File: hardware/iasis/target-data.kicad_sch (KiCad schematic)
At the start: 22 parts, among them J401 1054500101, U401 HD3SS3212IRKSR, U402 TPD4E02B04DQAR, U403 TPD4E02B04DQAR, U404 TPD6S300ARUKR, U405 FUSB302BMPX

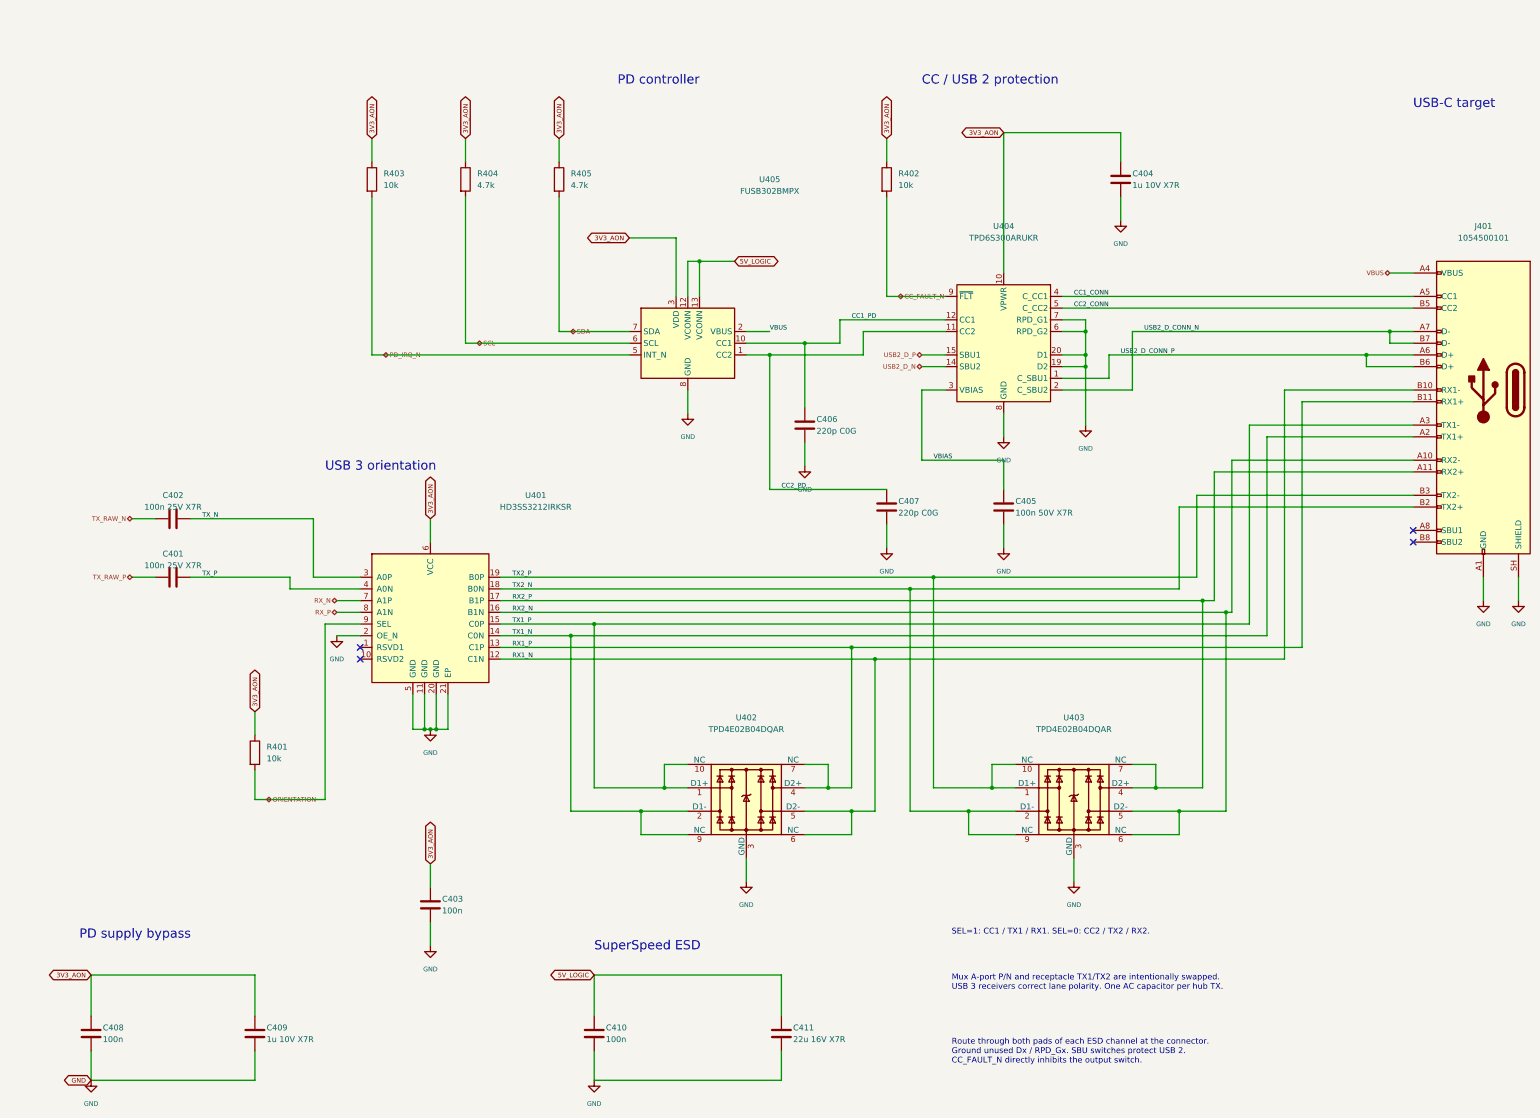
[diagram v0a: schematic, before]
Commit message: Redraw the target port sheets
The per-port data, output and charging sheets follow the signal and
power paths left to right. The receptacle sits at the right edge with
its CC and USB 2 protection wired to it, the SuperSpeed mux and ESD
arrays below, and the charging buck, feedback divider, OVP network and
output eFuse in one row. The port sheet joins its two blocks with
wires. The netlist is unchanged.
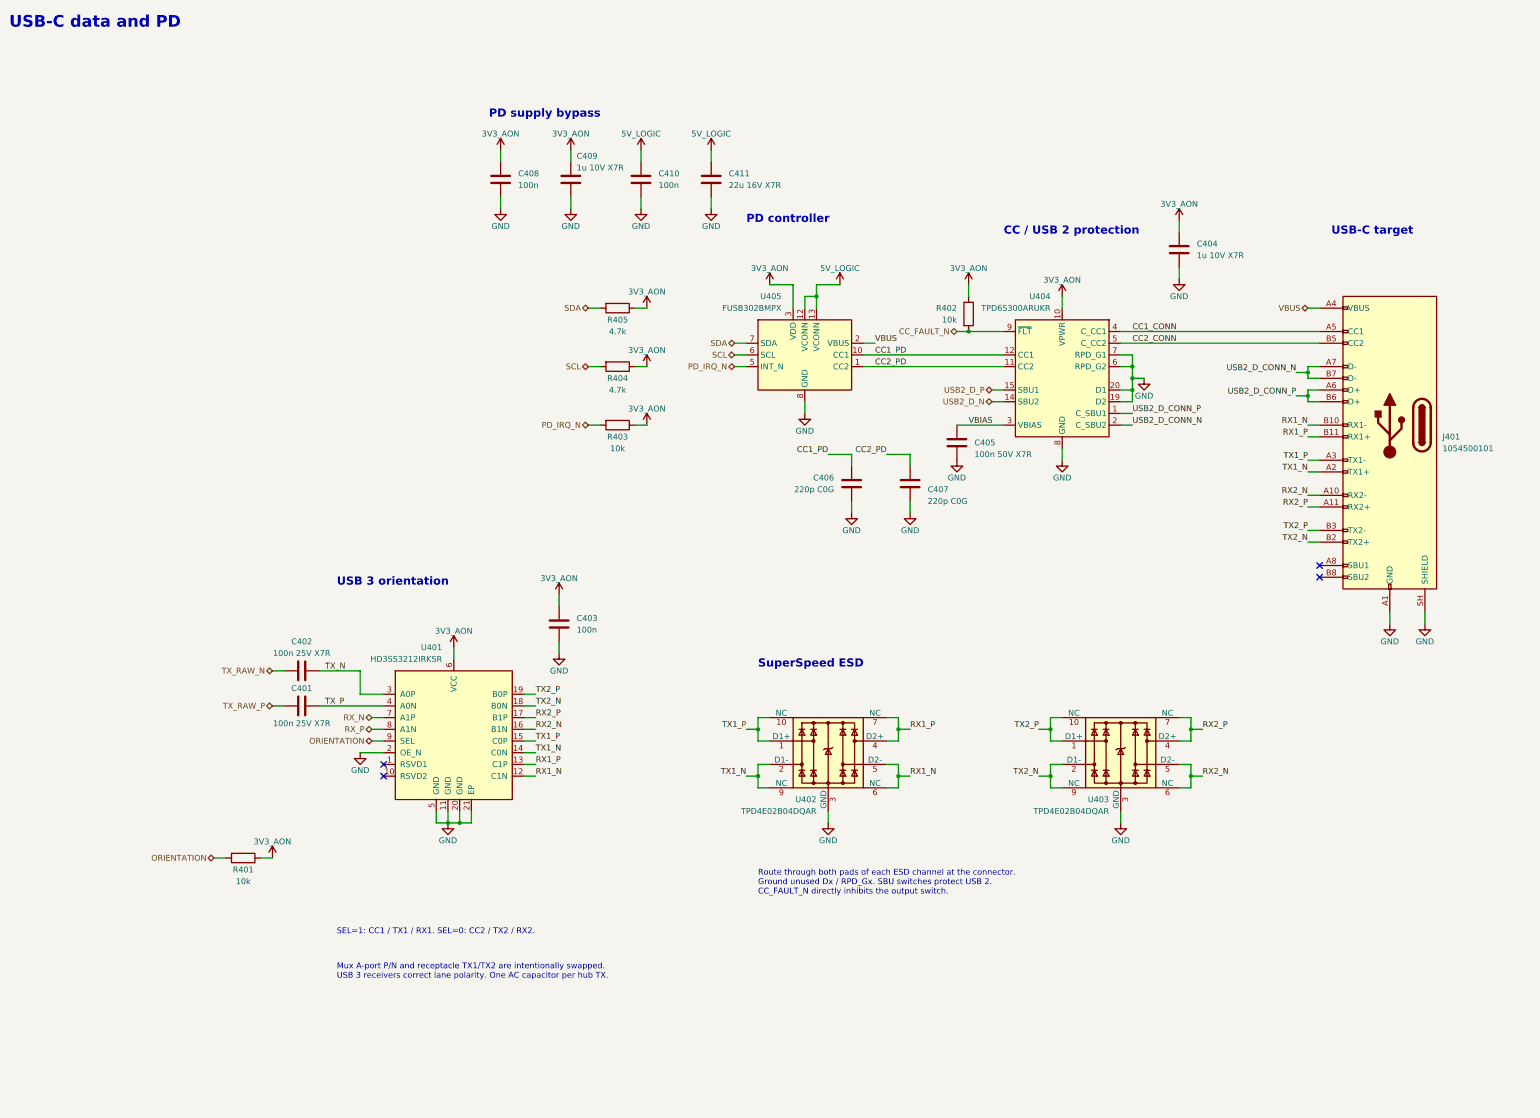
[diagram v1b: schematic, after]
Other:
- note added: "USB-C data and PD"
- moved on the sheet: C401, C402, C403, C404, C405, C406, C407, C408, C409, C410, C411, J401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

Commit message: Drill every via and thermal via at 0.3 mm
JLC prices 0.2 and 0.25 mm holes as a small-via tier that also forces
TG155 and a 4-wire Kelvin test: $39.18 on a five-board order. With
every plated hole at 0.3 mm or more the board quotes in the standard
tier.

- 2,005 vias keep their pads (0.45, 0.55, 0.6 mm) and drill 0.3 mm.
- U201's VQFN-100, the WQFN-20 and the HTSSOP-16 ThermalVias
  footprints move to Iasis.pretty copies with 0.3 mm thermal vias
  (121 holes); the schematic links follow.
- Rules match JLC's published via limits: 0.2 mm via hole to copper
  and hole to hole, 0.075 mm annular ring, 0.3 mm minimum hole.

DRC with refill and parity: 0 errors, 0 warnings, 0 unconnected.
Pour island counts unchanged; ERC unchanged at 14.
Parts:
- U404: footprint Package_DFN_QFN:WQFN-20-1EP_3x3mm_P0.4mm_EP1.7x1.7mm_ThermalVias -> Iasis:WQFN-20-1EP_3x3mm_P0.4mm_EP1.7x1.7mm_ThermalVias
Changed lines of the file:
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@@
 			)
 		)
-		(property "Footprint" "Package_DFN_QFN:WQFN-20-1EP_3x3mm_P0.4mm_EP1.7x1.7mm_ThermalVias"
+		(property "Footprint" "Iasis:WQFN-20-1EP_3x3mm_P0.4mm_EP1.7x1.7mm_ThermalVias"
 			(at 254 99.06 0)
 			(hide yes)
